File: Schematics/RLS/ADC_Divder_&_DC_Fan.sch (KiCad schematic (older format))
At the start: 11 parts, among them J7 DC_Fan, Q1 BS170

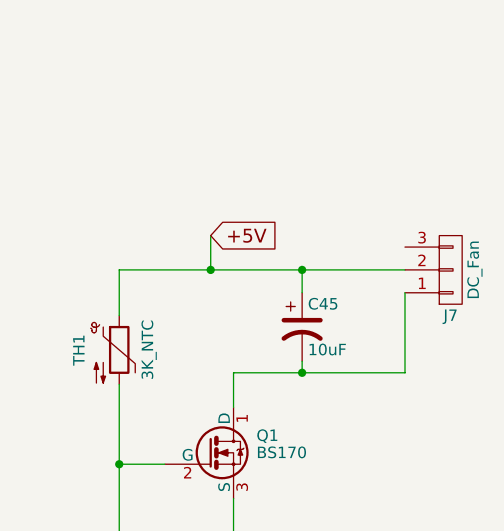
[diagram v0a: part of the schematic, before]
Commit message: Most Footprints Added
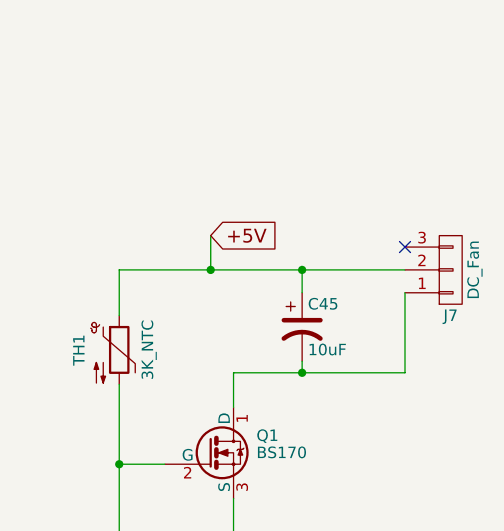
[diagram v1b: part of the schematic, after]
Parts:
- C45: footprint (none) -> Capacitors_SMD:CP_Elec_4x5.3
- J7: footprint (none) -> Pin_Headers:Pin_Header_Straight_1x03_Pitch2.54mm
- Q1: footprint TO_SOT_Packages_THT:TO-92_Molded_Narrow -> TO_SOT_Packages_SMD:SOT-23
- R11, R12, R13, R14, R15, R16, R29: footprint (none) -> Resistors_SMD:R_1206_HandSoldering
- TH1: footprint (none) -> Resistors_THT:R_Axial_DIN0411_L9.9mm_D3.6mm_P12.70mm_Horizontal
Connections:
- no-connect marks 0 -> 1
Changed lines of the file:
@@
 F 0 "R11" V 2180 1550 50  0000 C CNN
 F 1 "20K" V 2100 1550 50  0000 C CNN
-F 2 "" V 2030 1550 50  0001 C CNN
+F 2 "Resistors_SMD:R_1206_HandSoldering" V 2030 1550 50  0001 C CNN
 F 3 "" H 2100 1550 50  0001 C CNN
 	1    2100 1550
@@
 F 0 "R12" V 2430 1700 50  0000 C CNN
 F 1 "10K" V 2350 1700 50  0000 C CNN
-F 2 "" V 2280 1700 50  0001 C CNN
+F 2 "Resistors_SMD:R_1206_HandSoldering" V 2280 1700 50  0001 C CNN
 F 3 "" H 2350 1700 50  0001 C CNN
 	1    2350 1700
@@
 F 0 "R13" V 3080 1550 50  0000 C CNN
 F 1 "20K" V 3000 1550 50  0000 C CNN
-F 2 "" V 2930 1550 50  0001 C CNN
+F 2 "Resistors_SMD:R_1206_HandSoldering" V 2930 1550 50  0001 C CNN
 F 3 "" H 3000 1550 50  0001 C CNN
 	1    3000 1550
@@
 F 0 "R14" V 3330 1700 50  0000 C CNN
 F 1 "10K" V 3250 1700 50  0000 C CNN
-F 2 "" V 3180 1700 50  0001 C CNN
+F 2 "Resistors_SMD:R_1206_HandSoldering" V 3180 1700 50  0001 C CNN
 F 3 "" H 3250 1700 50  0001 C CNN
 	1    3250 1700
@@
 F 0 "R15" V 3980 1550 50  0000 C CNN
 F 1 "10K" V 3900 1550 50  0000 C CNN
-F 2 "" V 3830 1550 50  0001 C CNN
+F 2 "Resistors_SMD:R_1206_HandSoldering" V 3830 1550 50  0001 C CNN
 F 3 "" H 3900 1550 50  0001 C CNN
 	1    3900 1550
@@
 F 0 "R16" V 4230 1700 50  0000 C CNN
 F 1 "10K" V 4150 1700 50  0000 C CNN
-F 2 "" V 4080 1700 50  0001 C CNN
+F 2 "Resistors_SMD:R_1206_HandSoldering" V 4080 1700 50  0001 C CNN
 F 3 "" H 4150 1700 50  0001 C CNN
 	1    4150 1700
@@
 F 0 "Q1" H 7400 3025 50  0000 L CNN
 F 1 "BS170" H 7400 2950 50  0000 L CNN
-F 2 "TO_SOT_Packages_THT:TO-92_Molded_Narrow" H 7400 2875 50  0001 L CIN
+F 2 "TO_SOT_Packages_SMD:SOT-23" H 7400 2875 50  0001 L CIN
 F 3 "" H 7200 2950 50  0001 L CNN
 	1    7200 2950
@@
 F 0 "R29" V 6880 3450 50  0000 C CNN
 F 1 "1K" V 6800 3450 50  0000 C CNN
-F 2 "" V 6730 3450 50  0001 C CNN
+F 2 "Resistors_SMD:R_1206_HandSoldering" V 6730 3450 50  0001 C CNN
 F 3 "" H 6800 3450 50  0001 C CNN
 	1    6800 3450
@@
 F 0 "TH1" V 6625 2500 50  0000 C CNN
 F 1 "3K_NTC" V 6925 2500 50  0000 C CNN
-F 2 "" H 6800 2550 50  0001 C CNN
+F 2 "Resistors_THT:R_Axial_DIN0411_L9.9mm_D3.6mm_P12.70mm_Horizontal" H 6800 2550 50  0001 C CNN
 F 3 "" H 6800 2550 50  0001 C CNN
 	1    6800 2500
@@
 F 0 "C45" H 7625 2500 50  0000 L CNN
 F 1 "10uF" H 7625 2300 50  0000 L CNN
-F 2 "" H 7600 2400 50  0001 C CNN
+F 2 "Capacitors_SMD:CP_Elec_4x5.3" H 7600 2400 50  0001 C CNN
 F 3 "" H 7600 2400 50  0001 C CNN
 	1    7600 2400
@@
 F 0 "J7" H 8250 2350 50  0000 C CNN
 F 1 "DC_Fan" V 8350 2150 50  0000 C CNN
-F 2 "" H 8250 2150 50  0001 C CNN
+F 2 "Pin_Headers:Pin_Header_Straight_1x03_Pitch2.54mm" H 8250 2150 50  0001 C CNN
 F 3 "" H 8250 2150 50  0001 C CNN
 	1    8250 2150
@@
 	7050 3850 7050 3700
 Connection ~ 7050 3700
+NoConn ~ 8050 2050
 $EndSCHEMATC
